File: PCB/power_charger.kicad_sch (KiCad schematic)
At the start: 11 parts

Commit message: task: alert on Basic-library alternatives during JLC part matching (#33)
* task: alert on Basic-library alternatives during JLC part matching

JLC's "Extended" library carries a per-unique-part setup fee on top of
unit price; "Basic" doesn't. That fee doesn't amortize well on a board
with many distinct low-quantity parts -- confirmed the hard way: our
first real JLCPCB assembly quote came back at $333.84 vs PCBWay's
~$190 for the same order, and all 33 of our matched parts were
Extended.

jlc_match.py now does a secondary search for a same-value/same-package
Basic-library part whenever the real match lands on Extended, and
flags it in the report (new BasicAlt column + a Status alert) rather
than silently leaving it. On the current board this surfaces 11
plausible Basic-library swaps (common resistor/cap values, and the
generic 1N4148W diode and 2N7002 MOSFET, which are industry-standard
parts many brands stock identically).

This is alert-only, same as the rest of this script -- it doesn't
touch the schematic. Spot-checked 4 of the 11 suggestions directly
against JLC's catalog to confirm value/package actually match, not
just a keyword hit.

Co-Authored-By: Claude Sonnet 5 <noreply@anthropic.com>

* fix: two correctness bugs in Basic-library alternative matching

1. find_basic_alternative() trusted the raw keyword-search hit without
   verifying the candidate's actual value -- JLC's fuzzy full-text search
   can return a wrong-value part that just shares digits (e.g. searching
   "100 0402" surfaced a 1kΩ resistor, EIA code "1001", as a false match
   for a 100Ω part). Now parses and compares the actual numeric value
   (with unit) before accepting a candidate; falls back to exact
   model-name matching for non-numeric values (generic diode/transistor
   part families like "1N4148W", "2N7002").

2. The new value parser's regex required the unit to be the first
   character of the string, but JLC resistor descriptions carry a
   Chinese prefix ("厚膜电阻 10kΩ ±1%" = "thi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
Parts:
- C_BAT1, C_SYS_1, C_VIN_1: LCSC C6119886 -> C15850; MF HRE -> Samsung Electro-Mechanics; Manufacturer_Part_Number CGA0805X5R106K160MT -> CL21A106KAYNNNE
- C_SYS_2, C_VIN_2: LCSC C131394 -> C1525; MF Yageo -> Samsung Electro-Mechanics; Manufacturer_Part_Number CC0402KRX7R9BB104 -> CL05B104KO5NNNC
- R_STAT1, R_STAT2, R_TS1: LCSC C60490 -> C25744; MF Yageo -> UNI-ROYAL(Uniroyal Elec); Manufacturer_Part_Number RC0402FR-0710KL -> 0402WGF1002TCE
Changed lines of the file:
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@@
 			)
 		)
-		(property "MF" "Yageo"
-			(at 0 0 0)
-			(hide yes)
-			(show_name no)
-			(do_not_autoplace no)
-			(effects
-				(font
-					(size 1.27 1.27)
-				)
-			)
-		)
-		(property "Manufacturer_Part_Number" "CC0402KRX7R9BB104"
-			(at 0 0 0)
-			(hide yes)
-			(show_name no)
-			(do_not_autoplace no)
-			(effects
-				(font
-					(size 1.27 1.27)
-				)
-			)
-		)
-		(property "LCSC" "C131394"
+		(property "MF" "Samsung Electro-Mechanics"
+			(at 0 0 0)
+			(hide yes)
+			(show_name no)
+			(do_not_autoplace no)
+			(effects
+				(font
+					(size 1.27 1.27)
+				)
+			)
+		)
+		(property "Manufacturer_Part_Number" "CL05B104KO5NNNC"
+			(at 0 0 0)
+			(hide yes)
+			(show_name no)
+			(do_not_autoplace no)
+			(effects
+				(font
+					(size 1.27 1.27)
+				)
+			)
+		)
+		(property "LCSC" "C1525"
 			(at 0 0 0)
 			(hide yes)
@@
 			)
 		)
-		(property "MF" "Yageo"
-			(at 0 0 0)
-			(hide yes)
-			(show_name no)
-			(do_not_autoplace no)
-			(effects
-				(font
-					(size 1.27 1.27)
-				)
-			)
-		)
-		(property "Manufacturer_Part_Number" "RC0402FR-0710KL"
-			(at 0 0 0)
-			(hide yes)
-			(show_name no)
-			(do_not_autoplace no)
-			(effects
-				(font
-					(size 1.27 1.27)
-				)
-			)
-		)
-		(property "LCSC" "C60490"
+		(property "MF" "UNI-ROYAL(Uniroyal Elec)"
+			(at 0 0 0)
+			(hide yes)
+			(show_name no)
+			(do_not_autoplace no)
+			(effects
+				(font
+					(size 1.27 1.27)
+				)
+			)
+		)
+		(property "Manufacturer_Part_Number" "0402WGF1002TCE"
+			(at 0 0 0)
+			(hide yes)
+			(show_name no)
+			(do_not_autoplace no)
+			(effects
+				(font
+					(size 1.27 1.27)
+				)
+			)
+		)
+		(property "LCSC" "C25744"
 			(at 0 0 0)
 			(hide yes)
@@
 			)
 		)
-		(property "MF" "Yageo"
-			(at 0 0 0)
-			(hide yes)
-			(show_name no)
-			(do_not_autoplace no)
-			(effects
-				(font
-					(size 1.27 1.27)
-				)
-			)
-		)
-		(property "Manufacturer_Part_Number" "RC0402FR-0710KL"
-			(at 0 0 0)
-			(hide yes)
-			(show_name no)
-			(do_not_autoplace no)
-			(effects
-				(font
-					(size 1.27 1.27)
-				)
-			)
-		)
-		(property "LCSC" "C60490"
+		(property "MF" "UNI-ROYAL(Uniroyal Elec)"
+			(at 0 0 0)
+			(hide yes)
+			(show_name no)
+			(do_not_autoplace no)
+			(effects
+				(font
+					(size 1.27 1.27)
+				)
+			)
+		)
+		(property "Manufacturer_Part_Number" "0402WGF1002TCE"
+			(at 0 0 0)
+			(hide yes)
+			(show_name no)
+			(do_not_autoplace no)
+			(effects
+				(font
+					(size 1.27 1.27)
+				)
+			)
+		)
+		(property "LCSC" "C25744"
 			(at 0 0 0)
 			(hide yes)
@@
 			)
 		)
-		(property "MF" "HRE"
-			(at 0 0 0)
-			(hide yes)
-			(show_name no)
-			(do_not_autoplace no)
-			(effects
-				(font
-					(size 1.27 1.27)
-				)
-			)
-		)
-		(property "Manufacturer_Part_Number" "CGA0805X5R106K160MT"
-			(at 0 0 0)
-			(hide yes)
-			(show_name no)
-			(do_not_autoplace no)
-			(effects
-				(font
-					(size 1.27 1.27)
-				)
-			)
-		)
-		(property "LCSC" "C6119886"
+		(property "MF" "Samsung Electro-Mechanics"
+			(at 0 0 0)
+			(hide yes)
+			(show_name no)
+			(do_not_autoplace no)
+			(effects
+				(font
+					(size 1.27 1.27)
+				)
+			)
+		)
+		(property "Manufacturer_Part_Number" "CL21A106KAYNNNE"
+			(at 0 0 0)
+			(hide yes)
+			(show_name no)
+			(do_not_autoplace no)
+			(effects
+				(font
+					(size 1.27 1.27)
+				)
+			)
+		)
+		(property "LCSC" "C15850"
 			(at 0 0 0)
 			(hide yes)
@@
 			)
 		)
-		(property "MF" "HRE"
-			(at 0 0 0)
-			(hide yes)
-			(show_name no)
-			(do_not_autoplace no)
-			(effects
-				(font
-					(size 1.27 1.27)
-				)
-			)
-		)
-		(property "Manufacturer_Part_Number" "CGA0805X5R106K160MT"
-			(at 0 0 0)
-			(hide yes)
-			(show_name no)
-			(do_not_autoplace no)
-			(effects
-				(font
-					(size 1.27 1.27)
-				)
-			)
-		)
-		(property "LCSC" "C6119886"
+		(property "MF" "Samsung Electro-Mechanics"
+			(at 0 0 0)
+			(hide yes)
+			(show_name no)
+			(do_not_autoplace no)
+			(effects
+				(font
+					(size 1.27 1.27)
+				)
+			)
+		)
+		(property "Manufacturer_Part_Number" "CL21A106KAYNNNE"
+			(at 0 0 0)
+			(hide yes)
+			(show_name no)
+			(do_not_autoplace no)
+			(effects
+				(font
+					(size 1.27 1.27)
+				)
+			)
+		)
+		(property "LCSC" "C15850"
 			(at 0 0 0)
 			(hide yes)
@@
 			)
 		)
-		(property "MF" "Yageo"
-			(at 0 0 0)
-			(hide yes)
-			(show_name no)
-			(do_not_autoplace no)
-			(effects
-				(font
-					(size 1.27 1.27)
-				)
-			)
-		)
-		(property "Manufacturer_Part_Number" "CC0402KRX7R9BB104"
-			(at 0 0 0)
-			(hide yes)
-			(show_name no)
-			(do_not_autoplace no)
-			(effects
-				(font
-					(size 1.27 1.27)
-				)
-			)
-		)
-		(property "LCSC" "C131394"
+		(property "MF" "Samsung Electro-Mechanics"
+			(at 0 0 0)
+			(hide yes)
+			(show_name no)
+			(do_not_autoplace no)
+			(effects
+				(font
+					(size 1.27 1.27)
+				)
+			)
+		)
+		(property "Manufacturer_Part_Number" "CL05B104KO5NNNC"
+			(at 0 0 0)
+			(hide yes)
+			(show_name no)
+			(do_not_autoplace no)
+			(effects
+				(font
+					(size 1.27 1.27)
+				)
+			)
+		)
+		(property "LCSC" "C1525"
 			(at 0 0 0)
 			(hide yes)
@@
 			)
 		)
-		(property "MF" "HRE"
-			(at 0 0 0)
-			(hide yes)
-			(show_name no)
-			(do_not_autoplace no)
-			(effects
-				(font
-					(size 1.27 1.27)
-				)
-			)
-		)
-		(property "Manufacturer_Part_Number" "CGA0805X5R106K160MT"
-			(at 0 0 0)
-			(hide yes)
-			(show_name no)
-			(do_not_autoplace no)
-			(effects
-				(font
-					(size 1.27 1.27)
-				)
-			)
-		)
-		(property "LCSC" "C6119886"
+		(property "MF" "Samsung Electro-Mechanics"
+			(at 0 0 0)
+			(hide yes)
+			(show_name no)
+			(do_not_autoplace no)
+			(effects
+				(font
+					(size 1.27 1.27)
+				)
+			)
+		)
+		(property "Manufacturer_Part_Number" "CL21A106KAYNNNE"
+			(at 0 0 0)
+			(hide yes)
+			(show_name no)
+			(do_not_autoplace no)
+			(effects
+				(font
+					(size 1.27 1.27)
+				)
+			)
+		)
+		(property "LCSC" "C15850"
 			(at 0 0 0)
 			(hide yes)
@@
 			)
 		)
-		(property "MF" "Yageo"
-			(at 0 0 0)
-			(hide yes)
-			(show_name no)
-			(do_not_autoplace no)
-			(effects
-				(font
-					(size 1.27 1.27)
-				)
-			)
-		)
-		(property "Manufacturer_Part_Number" "RC0402FR-0710KL"
-			(at 0 0 0)
-			(hide yes)
-			(show_name no)
-			(do_not_autoplace no)
-			(effects
-				(font
-					(size 1.27 1.27)
-				)
-			)
-		)
-		(property "LCSC" "C60490"
-			(at 0 0 0)
-			(hide yes)
+		(property "MF" "UNI-ROYAL(Uniroyal Elec)"
+			(at 0 0 0)
+			(hide yes)
+			(show_name no)
+			(do_not_autoplace no)
+			(effects
+				(font
+					(size 1.27 1.27)
+				)
+			)
+		)
+		(property "Manufacturer_Part_Number" "0402WGF1002TCE"
+			(at 0 0 0)
+			(hide yes)
+			(show_name no)
+			(do_not_autoplace no)
+			(effects
+				(font
+					(size 1.27 1.27)
+				)
+			)
+		)
+		(property "LCSC" "C25744"
+			(at 0 0 0)
+			(hide yes)

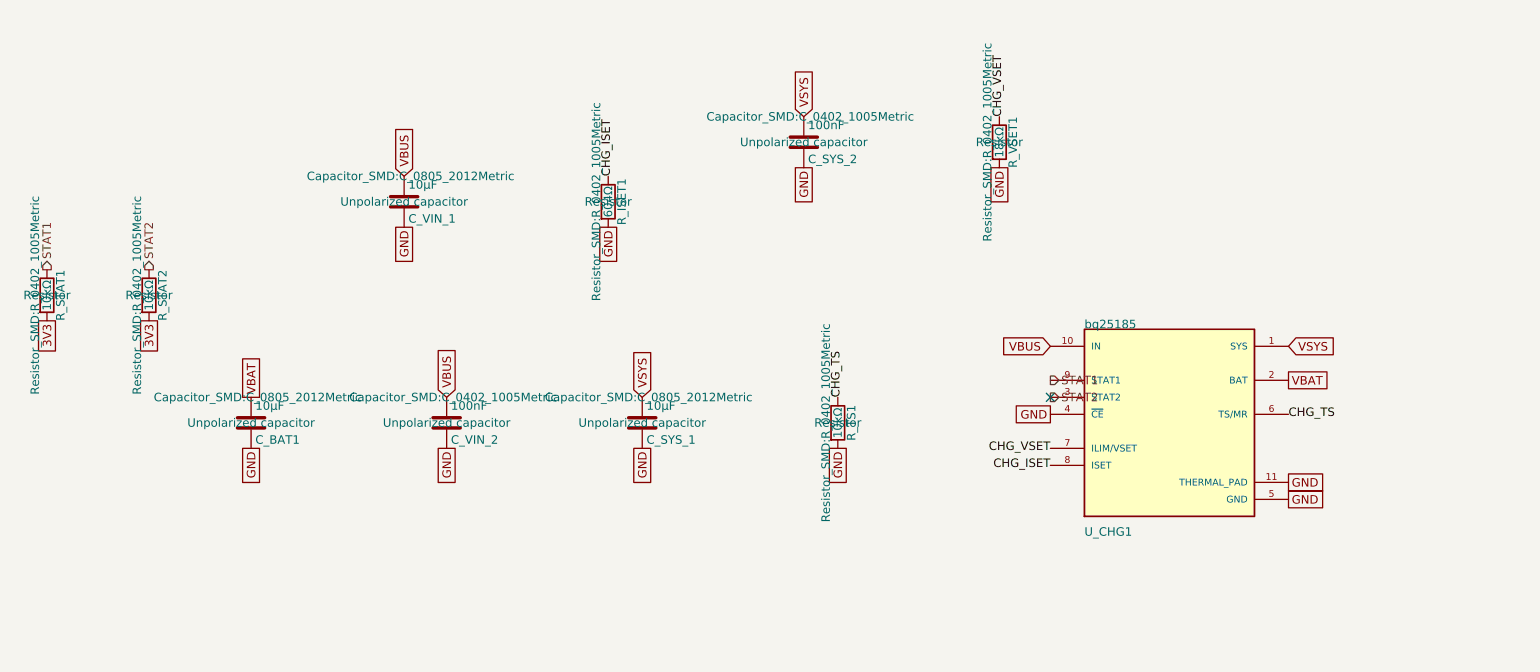
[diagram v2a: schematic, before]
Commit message: fix: make every BOM Value unambiguous for the fab, and switch D_INV_ISO1 to SOT-323 (#61)
* fix: make every BOM Value unambiguous for the fab, and switch D_INV_ISO1 to SOT-323

PCBWay flagged D_INV_ISO1: "BAT54W" is SOT-323 from nearly every maker, but we
had picked Yangjie's SOD-123 variant. A fab only sees Designator, Footprint,
Quantity and Value in the BOM (never MF/MPN/LCSC), so a bare part name is
ambiguous. Fixes the class of problem, not just this part:

- Every component's Value is now "<label> | <MPN> | <manufacturer> | <package>"
  (label dropped when it repeats the MPN; commas/periods stripped so the CSV
  never needs quoting). BT1 keeps its RIGHT-ANGLE HORIZONTAL note. Applied to
  all 81 parts across every sheet and the PCB.
- scripts/bom_values.py builds, applies, and checks these values, including
  that the PCB copy of Value/MF/MPN/footprint matches the schematic. New
  footprints must be added to its package table on purpose; hand-sourced parts
  with no MPN (J_STICK1) are listed explicitly.
- D_INV_ISO1 -> Diodes BAT54W-7-F in SOT-323 (common part, several makers).
  Pin 1 anode / pin 2 not connected / pin 3 cathode, confirmed against
  Nexperia's numbered pinning table and Diodes' datasheet. Uses KiCad's
  Diode:BAT54W symbol; PCB footprint replaced and rerouted. Electrically the
  same BAT54 family (30V, 200mA, 2uA leakage at 25V), so the SPICE model and
  scripts/spice/latch_sim.py still pass.
- Layout diagrams now say AO3401A for Q_PWR1 (they were stale since it was
  swapped from DMG2305UX) and BAT54W-7-F/SOT-323 for D_INV_ISO1.
- Repo CLAUDE.md documents the Value rule and the script.

ERC/DRC clean; production files regenerated.

Co-Authored-By: Claude Sonnet 5 <noreply@anthropic.com>

* chore: commit KiCad project settings (reordered used-designators list)

Co-Authored-By: Claude Sonnet 5 <noreply@anthropic.com>

---------

Co-authored-by: Claude Sonnet 5 <noreply@anthropic.com>
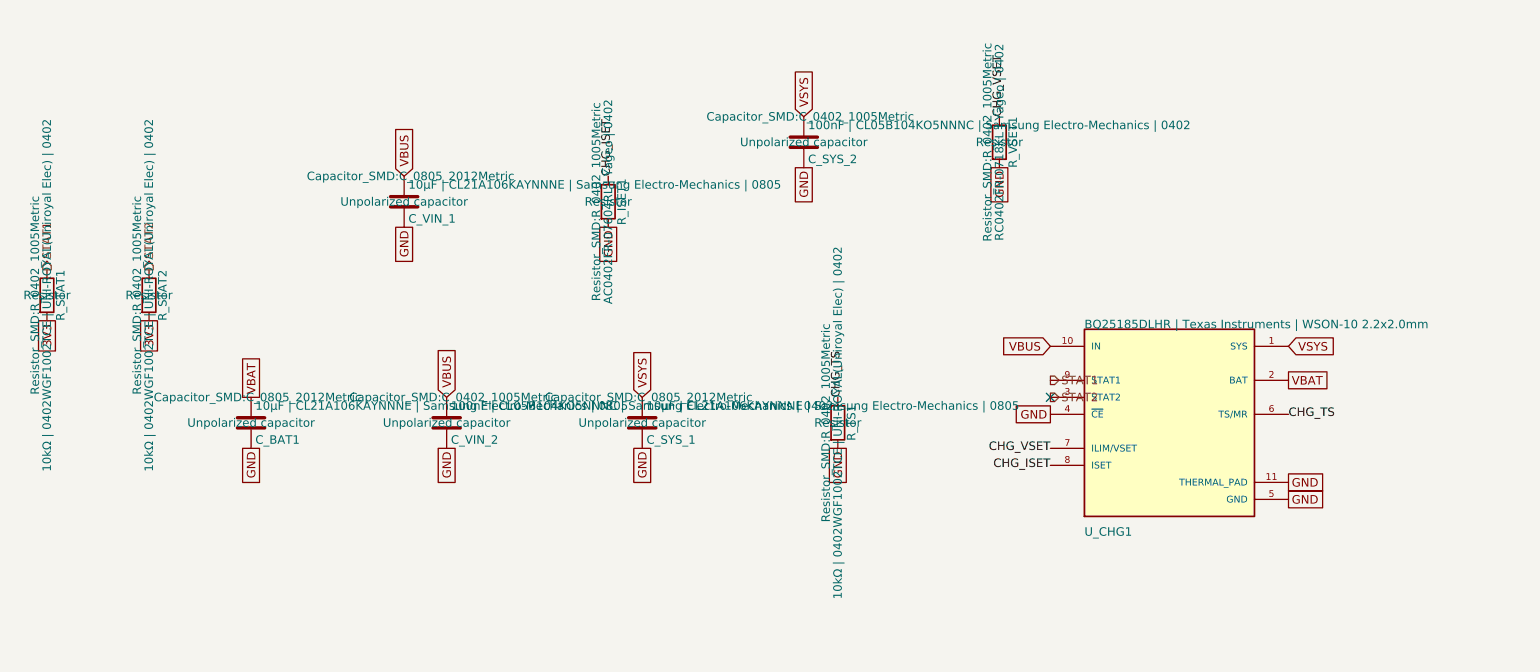
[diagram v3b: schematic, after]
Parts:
- C_BAT1, C_SYS_1, C_VIN_1: value 10µF -> 10µF | CL21A106KAYNNNE | Samsung Electro-Mechanics | 0805
- C_SYS_2, C_VIN_2: value 100nF -> 100nF | CL05B104KO5NNNC | Samsung Electro-Mechanics | 0402
- R_ISET1: value 604Ω -> AC0402FR-07604RL | Yageo | 0402
- R_STAT1, R_STAT2, R_TS1: value 10kΩ -> 10kΩ | 0402WGF1002TCE | UNI-ROYAL(Uniroyal Elec) | 0402
- R_VSET1: value 18kΩ -> RC0402FR-0718KL | Yageo | 0402
- U_CHG1: value bq25185 -> BQ25185DLHR | Texas Instruments | WSON-10 2.2x2.0mm
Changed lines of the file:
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@@
 			)
 		)
-		(property "Value" "18kΩ"
+		(property "Value" "RC0402FR-0718KL | Yageo | 0402"
 			(at 207.01 83.82 90)
 			(show_name no)
@@
 			)
 		)
-		(property "Value" "100nF"
+		(property "Value" "100nF | CL05B104KO5NNNC | Samsung Electro-Mechanics | 0402"
 			(at 178.435 81.28 0)
 			(show_name no)
@@
 			)
 		)
-		(property "Value" "10kΩ"
+		(property "Value" "10kΩ | 0402WGF1002TCE | UNI-ROYAL(Uniroyal Elec) | 0402"
 			(at 64.77 106.68 90)
 			(show_name no)
@@
 			)
 		)
-		(property "Value" "10µF"
+		(property "Value" "10µF | CL21A106KAYNNNE | Samsung Electro-Mechanics | 0805"
 			(at 154.305 123.19 0)
 			(show_name no)
@@
 			)
 		)
-		(property "Value" "bq25185"
+		(property "Value" "BQ25185DLHR | Texas Instruments | WSON-10 2.2x2.0mm"
 			(at 219.71 111.76 0)
 			(show_name no)
@@
 			)
 		)
-		(property "Value" "10µF"
+		(property "Value" "10µF | CL21A106KAYNNNE | Samsung Electro-Mechanics | 0805"
 			(at 95.885 123.19 0)
 			(show_name no)
@@
 			)
 		)
-		(property "Value" "100nF"
+		(property "Value" "100nF | CL05B104KO5NNNC | Samsung Electro-Mechanics | 0402"
 			(at 125.095 123.19 0)
 			(show_name no)
@@
 			)
 		)
-		(property "Value" "604Ω"
+		(property "Value" "AC0402FR-07604RL | Yageo | 0402"
 			(at 148.59 92.71 90)
 			(show_name no)
@@
 			)
 		)
-		(property "Value" "10µF"
+		(property "Value" "10µF | CL21A106KAYNNNE | Samsung Electro-Mechanics | 0805"
 			(at 118.745 90.17 0)
 			(show_name no)
@@
 			)
 		)
-		(property "Value" "10kΩ"
+		(property "Value" "10kΩ | 0402WGF1002TCE | UNI-ROYAL(Uniroyal Elec) | 0402"
 			(at 80.01 106.68 90)
 			(show_name no)
@@
 			)
 		)
-		(property "Value" "10kΩ"
+		(property "Value" "10kΩ | 0402WGF1002TCE | UNI-ROYAL(Uniroyal Elec) | 0402"
 			(at 182.88 125.73 90)
 			(show_name no)
